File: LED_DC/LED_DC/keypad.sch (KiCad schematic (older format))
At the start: 4 parts

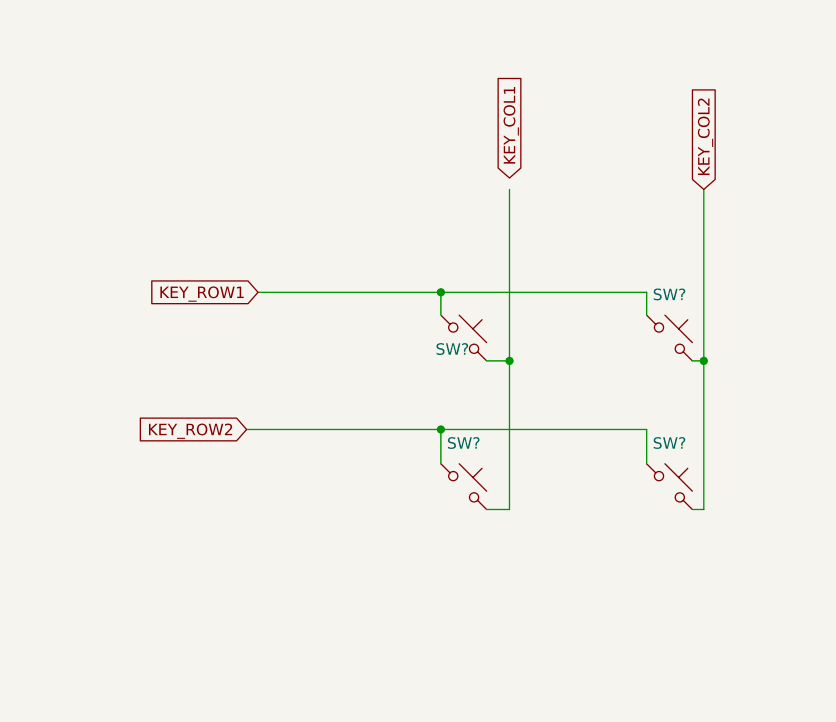
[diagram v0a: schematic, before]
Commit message: Added foot prints for the components.
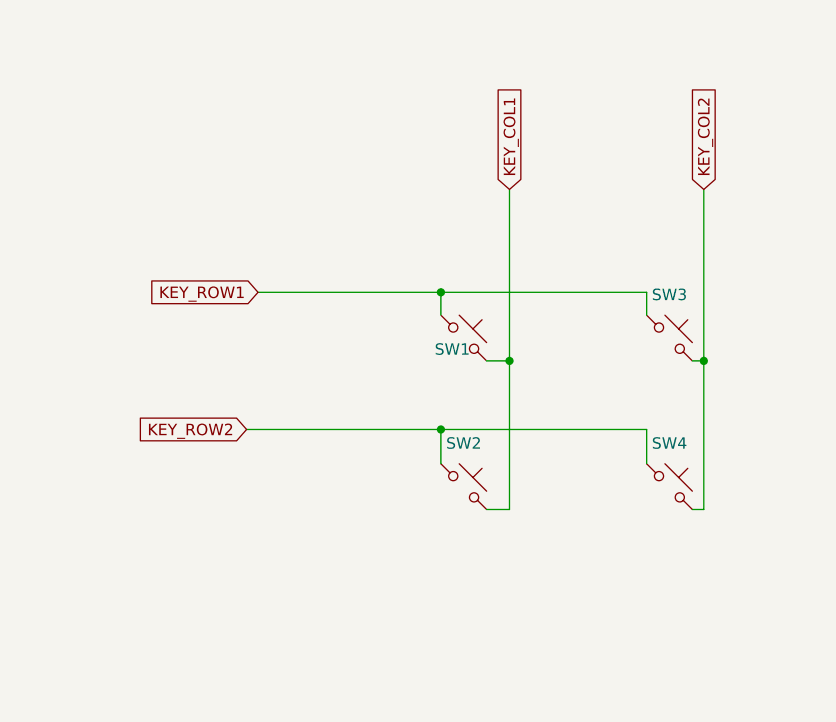
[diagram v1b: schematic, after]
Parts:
- SW1, SW2, SW3, SW4: renamed from SW?; footprint (none) -> Button_Switch_THT:SW_PUSH_6mm
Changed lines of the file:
@@
 $EndDescr
 $Comp
-L Switch:SW_Push_45deg SW?
+L Switch:SW_Push_45deg SW1
 U 1 1 5FEC2884
 P 3750 2950
-F 0 "SW?" H 3700 2900 50  0000 C CNN
+F 0 "SW1" H 3700 2900 50  0000 C CNN
 F 1 "SW_Push_45deg" H 3750 3140 50  0001 C CNN
-F 2 "" H 3750 2950 50  0001 C CNN
+F 2 "Button_Switch_THT:SW_PUSH_6mm" H 3750 2950 50  0001 C CNN
 F 3 "~" H 3750 2950 50  0001 C CNN
 	1    3750 2950
@@
 $EndComp
 $Comp
-L Switch:SW_Push_45deg SW?
+L Switch:SW_Push_45deg SW3
 U 1 1 5FEC3564
 P 4650 2950
-F 0 "SW?" H 4650 3139 50  0000 C CNN
+F 0 "SW3" H 4650 3139 50  0000 C CNN
 F 1 "SW_Push_45deg" H 4650 3140 50  0001 C CNN
-F 2 "" H 4650 2950 50  0001 C CNN
+F 2 "Button_Switch_THT:SW_PUSH_6mm" H 4650 2950 50  0001 C CNN
 F 3 "~" H 4650 2950 50  0001 C CNN
 	1    4650 2950
@@
 $EndComp
 $Comp
-L Switch:SW_Push_45deg SW?
+L Switch:SW_Push_45deg SW2
 U 1 1 5FEC4C0B
 P 3750 3600
-F 0 "SW?" H 3750 3789 50  0000 C CNN
+F 0 "SW2" H 3750 3789 50  0000 C CNN
 F 1 "SW_Push_45deg" H 3750 3790 50  0001 C CNN
-F 2 "" H 3750 3600 50  0001 C CNN
+F 2 "Button_Switch_THT:SW_PUSH_6mm" H 3750 3600 50  0001 C CNN
 F 3 "~" H 3750 3600 50  0001 C CNN
 	1    3750 3600
@@
 $EndComp
 $Comp
-L Switch:SW_Push_45deg SW?
+L Switch:SW_Push_45deg SW4
 U 1 1 5FEC4C11
 P 4650 3600
-F 0 "SW?" H 4650 3789 50  0000 C CNN
+F 0 "SW4" H 4650 3789 50  0000 C CNN
 F 1 "SW_Push_45deg" H 4650 3790 50  0001 C CNN
-F 2 "" H 4650 3600 50  0001 C CNN
+F 2 "Button_Switch_THT:SW_PUSH_6mm" H 4650 3600 50  0001 C CNN
 F 3 "~" H 4650 3600 50  0001 C CNN
 	1    4650 3600
@@
 Text GLabel 2800 3350 0    50   Input ~ 0
 KEY_ROW2
-Text GLabel 3950 2250 1    50   Input ~ 0
+Text GLabel 3950 2300 1    50   Input ~ 0
 KEY_COL1
 Text GLabel 4800 2300 1    50   Input ~ 0
@@
 	3650 3350 4550 3350
 Wire Wire Line
-	3950 2300 3950 3050
-Wire Wire Line
 	3950 3700 3850 3700
 Wire Wire Line
@@
 	4800 3700 4800 3050
 Connection ~ 4800 3050
+Wire Wire Line
+	3950 2300 3950 3050
 $EndSCHEMATC

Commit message: Added text to the schematic sections.
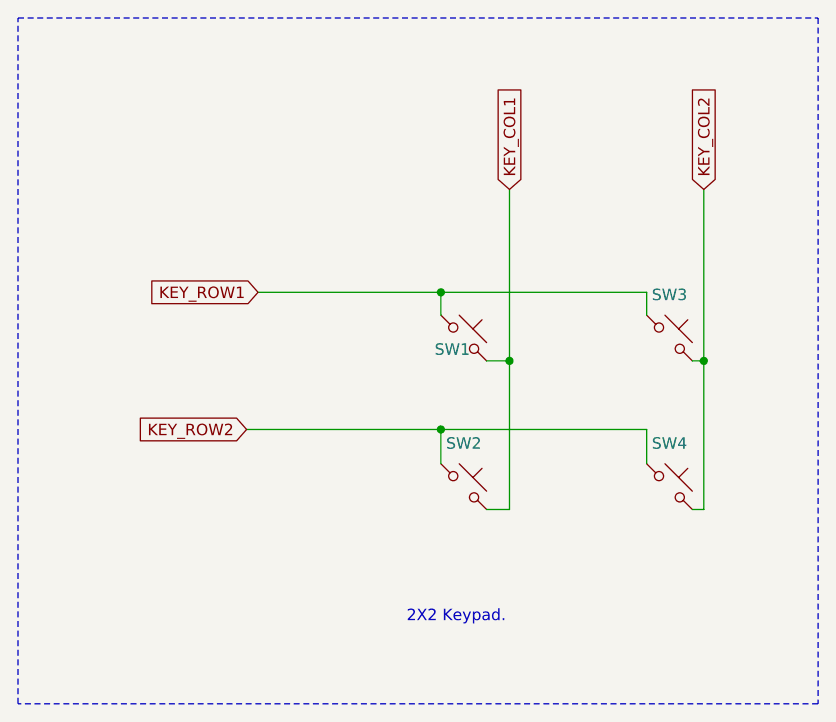
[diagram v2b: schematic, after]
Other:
- note added: "2X2 Keypad."
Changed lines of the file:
@@
 Wire Wire Line
 	3950 2300 3950 3050
+Wire Notes Line
+	5300 1550 5300 4550
+Wire Notes Line
+	5300 4550 1800 4550
+Wire Notes Line
+	1800 4550 1800 1550
+Wire Notes Line
+	1800 1550 5300 1550
+Text Notes 3500 4200 0    50   ~ 0
+2X2 Keypad.
 $EndSCHEMATC

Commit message: Updated component values.
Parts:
- SW1, SW2, SW3, SW4: value SW_Push_45deg -> Tactile switch 6mm
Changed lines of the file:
@@
 P 3750 2950
 F 0 "SW1" H 3700 2900 50  0000 C CNN
-F 1 "SW_Push_45deg" H 3750 3140 50  0001 C CNN
+F 1 "Tactile switch 6mm" H 3750 3140 50  0001 C CNN
 F 2 "Button_Switch_THT:SW_PUSH_6mm" H 3750 2950 50  0001 C CNN
 F 3 "~" H 3750 2950 50  0001 C CNN
@@
 P 4650 2950
 F 0 "SW3" H 4650 3139 50  0000 C CNN
-F 1 "SW_Push_45deg" H 4650 3140 50  0001 C CNN
+F 1 "Tactile switch 6mm" H 4650 3140 50  0001 C CNN
 F 2 "Button_Switch_THT:SW_PUSH_6mm" H 4650 2950 50  0001 C CNN
 F 3 "~" H 4650 2950 50  0001 C CNN
@@
 P 3750 3600
 F 0 "SW2" H 3750 3789 50  0000 C CNN
-F 1 "SW_Push_45deg" H 3750 3790 50  0001 C CNN
+F 1 "Tactile switch 6mm" H 3750 3790 50  0001 C CNN
 F 2 "Button_Switch_THT:SW_PUSH_6mm" H 3750 3600 50  0001 C CNN
 F 3 "~" H 3750 3600 50  0001 C CNN
@@
 P 4650 3600
 F 0 "SW4" H 4650 3789 50  0000 C CNN
-F 1 "SW_Push_45deg" H 4650 3790 50  0001 C CNN
+F 1 "Tactile switch 6mm" H 4650 3790 50  0001 C CNN
 F 2 "Button_Switch_THT:SW_PUSH_6mm" H 4650 3600 50  0001 C CNN
 F 3 "~" H 4650 3600 50  0001 C CNN
